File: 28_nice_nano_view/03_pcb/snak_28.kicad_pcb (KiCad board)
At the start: 2 copper layers, 114.8 x 99.6 mm, 156 parts

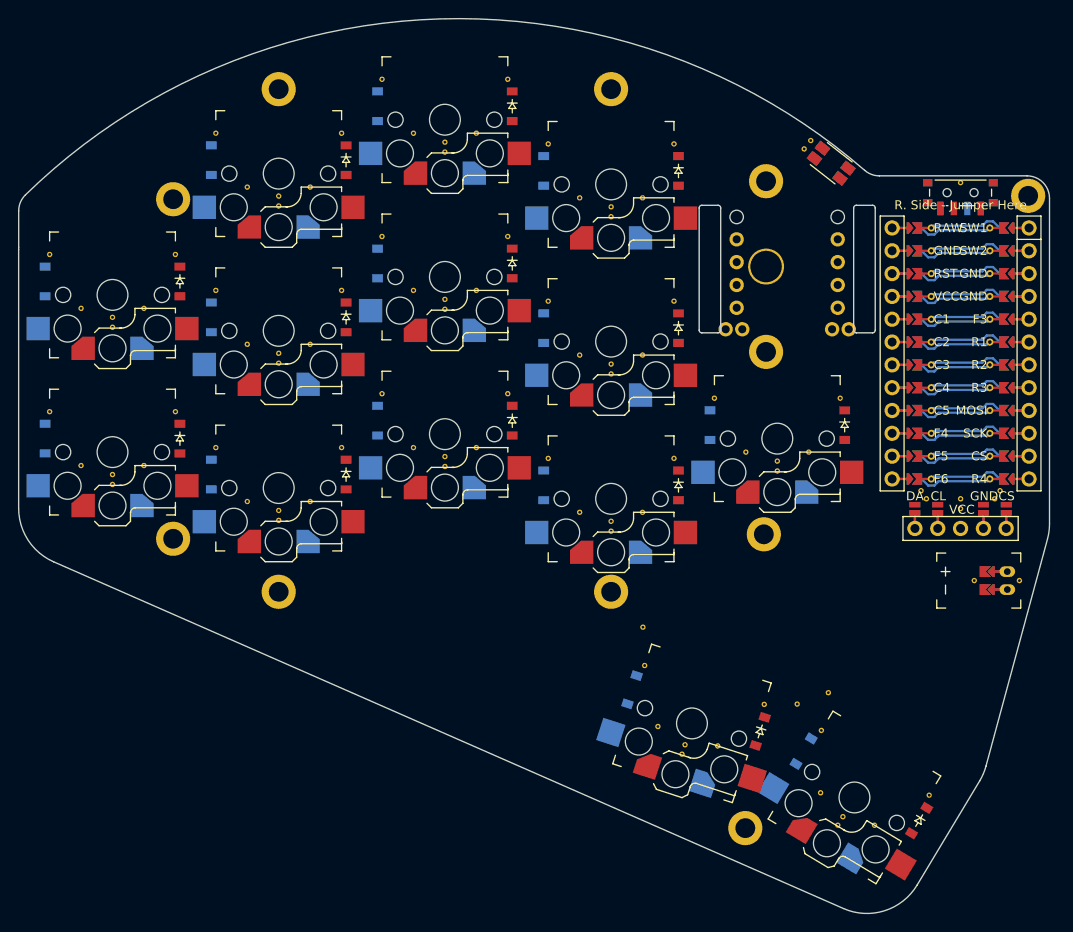
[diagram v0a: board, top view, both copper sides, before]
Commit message: add traces lib
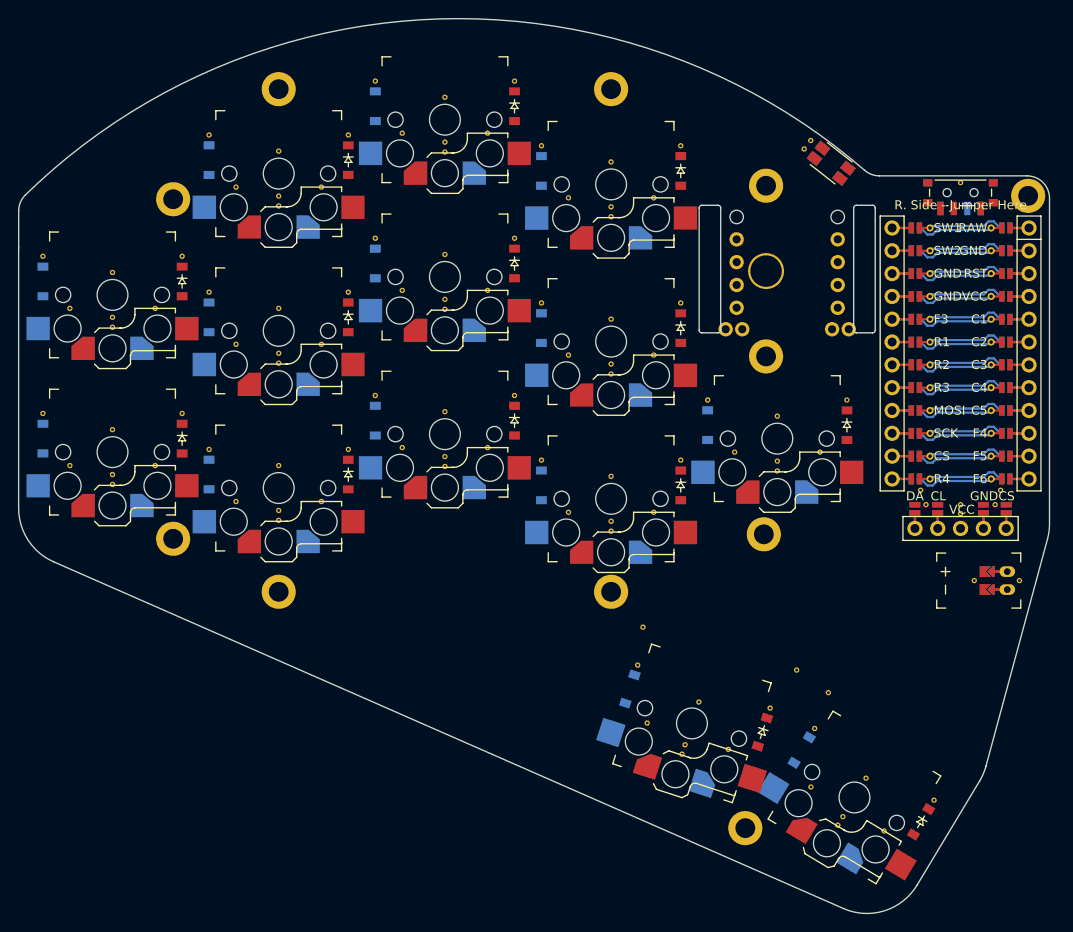
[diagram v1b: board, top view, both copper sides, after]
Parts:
- removed the REF** at (107.0, 78.0)
- removed the REF** at (162.5, 65.7)
- removed the REF** at (162.5, 48.2)
- removed the REF** at (181.0, 76.5)
- removed the REF** at (172.5, 110.6)
- removed the REF** at (190.9, 120.7)
- removed the REF** at (103.5, 84.0)
- removed the REF** at (103.5, 66.5)
- removed the REF** at (122.0, 88.0)
- removed the REF** at (122.0, 70.5)
- removed the REF** at (122.0, 53.0)
- removed the REF** at (107.0, 60.5)
- removed the REF** at (140.5, 82.0)
- removed the REF** at (140.5, 64.5)
- removed the REF** at (140.5, 47.0)
- removed the REF** at (159.0, 89.2)
- removed the REF** at (159.0, 71.7)
- removed the REF** at (159.0, 54.2)
- removed the REF** at (177.5, 82.5)
- removed the REF** at (167.4, 115.2)
- removed the REF** at (184.8, 124.0)
- removed the REF** at (93.0, 78.0)
- removed the REF** at (125.5, 82.0)
- removed the REF** at (93.0, 60.5)
- removed the REF** at (111.5, 82.0)
- removed the REF** at (111.5, 64.5)
- removed the REF** at (111.5, 47.0)
- removed the REF** at (130.0, 76.0)
- removed the REF** at (130.0, 58.5)
- removed the REF** at (130.0, 41.0)
- removed the REF** at (148.5, 83.2)
- removed the REF** at (148.5, 65.7)
- removed the REF** at (148.5, 48.2)
- removed the REF** at (125.5, 64.5)
- removed the REF** at (167.0, 76.5)
- removed the REF** at (159.2, 106.3)
- removed the REF** at (178.9, 113.5)
- removed the REF** at (96.5, 84.0)
- removed the REF** at (96.5, 66.5)
- removed the REF** at (115.0, 88.0)
- removed the REF** at (115.0, 70.5)
- removed the REF** at (115.0, 53.0)
- removed the REF** at (133.5, 82.0)
- removed the REF** at (133.5, 64.5)
- removed the REF** at (125.5, 47.0)
- removed the REF** at (133.5, 47.0)
- removed the REF** at (152.0, 89.2)
- removed the REF** at (152.0, 71.7)
- removed the REF** at (152.0, 54.2)
- removed the REF** at (170.5, 82.5)
- removed the REF** at (160.7, 113.0)
- removed the REF** at (178.8, 120.4)
- removed the REF** at (144.0, 76.0)
- removed the REF** at (144.0, 58.5)
- removed the REF** at (144.0, 41.0)
- removed the REF** at (176.2, 110.5)
- removed the REF** at (190.0, 86.8)
- removed the REF** at (198.8, 86.8)
- removed the REF** at (162.5, 83.2)
- removed the REF** at (194.4, 87.7)
- removed the REF** at (190.6, 87.7)
- removed the REF** at (198.2, 87.7)
- removed the REF** at (194.4, 88.8)
- added REF**: VIA-0.6mm, VIA-0.6mm, F.Cu at (107.8, 78.2)
- added REF**: VIA-0.6mm, VIA-0.6mm, F.Cu at (163.2, 65.9)
- added REF**: VIA-0.6mm, VIA-0.6mm, F.Cu at (190.0, 86.8)
- added REF**: VIA-0.6mm, VIA-0.6mm, F.Cu at (198.8, 86.8)
- added REF**: VIA-0.6mm, VIA-0.6mm, F.Cu at (190.6, 88.3)
- added REF**: VIA-0.6mm, VIA-0.6mm, F.Cu at (198.2, 88.3)
- added REF**: VIA-0.6mm, VIA-0.6mm, F.Cu at (194.4, 88.3)
- added REF**: VIA-0.6mm, VIA-0.6mm, F.Cu at (194.4, 89.3)
- added REF**: VIA-0.6mm, VIA-0.6mm, F.Cu at (163.2, 48.4)
- added REF**: VIA-0.6mm, VIA-0.6mm, F.Cu at (181.8, 76.7)
- added REF**: VIA-0.6mm, VIA-0.6mm, F.Cu at (173.2, 111.0)
- added REF**: VIA-0.6mm, VIA-0.6mm, F.Cu at (191.4, 121.2)
- added REF**: VIA-0.6mm, VIA-0.6mm, F.Cu at (104.8, 84.0)
- added REF**: VIA-0.6mm, VIA-0.6mm, F.Cu at (104.8, 66.5)
- added REF**: VIA-0.6mm, VIA-0.6mm, F.Cu at (123.2, 88.0)
- added REF**: VIA-0.6mm, VIA-0.6mm, F.Cu at (123.2, 70.5)
- added REF**: VIA-0.6mm, VIA-0.6mm, F.Cu at (123.2, 53.0)
- added REF**: VIA-0.6mm, VIA-0.6mm, F.Cu at (107.8, 60.7)
- added REF**: VIA-0.6mm, VIA-0.6mm, F.Cu at (141.8, 82.0)
- added REF**: VIA-0.6mm, VIA-0.6mm, F.Cu at (141.8, 64.5)
- added REF**: VIA-0.6mm, VIA-0.6mm, F.Cu at (141.8, 47.0)
- added REF**: VIA-0.6mm, VIA-0.6mm, F.Cu at (160.2, 89.2)
- added REF**: VIA-0.6mm, VIA-0.6mm, F.Cu at (160.2, 71.7)
- added REF**: VIA-0.6mm, VIA-0.6mm, F.Cu at (160.2, 54.2)
- added REF**: VIA-0.6mm, VIA-0.6mm, F.Cu at (178.8, 82.5)
- added REF**: VIA-0.6mm, VIA-0.6mm, F.Cu at (168.6, 115.6)
- added REF**: VIA-0.6mm, VIA-0.6mm, F.Cu at (185.9, 124.7)
- added REF**: VIA-0.6mm, VIA-0.6mm, F.Cu at (92.2, 78.2)
- added REF**: VIA-0.6mm, VIA-0.6mm, F.Cu at (126.2, 82.2)
- added REF**: VIA-0.6mm, VIA-0.6mm, F.Cu at (92.2, 60.7)
- added REF**: VIA-0.6mm, VIA-0.6mm, F.Cu at (110.8, 82.2)
- added REF**: VIA-0.6mm, VIA-0.6mm, F.Cu at (110.8, 64.7)
- added REF**: VIA-0.6mm, VIA-0.6mm, F.Cu at (110.8, 47.2)
- added REF**: VIA-0.6mm, VIA-0.6mm, F.Cu at (129.2, 76.2)
- added REF**: VIA-0.6mm, VIA-0.6mm, F.Cu at (129.2, 58.7)
- added REF**: VIA-0.6mm, VIA-0.6mm, F.Cu at (129.2, 41.2)
- added REF**: VIA-0.6mm, VIA-0.6mm, F.Cu at (147.8, 83.4)
- added REF**: VIA-0.6mm, VIA-0.6mm, F.Cu at (147.8, 65.9)
- added REF**: VIA-0.6mm, VIA-0.6mm, F.Cu at (147.8, 48.4)
- added REF**: VIA-0.6mm, VIA-0.6mm, F.Cu at (126.2, 64.7)
- added REF**: VIA-0.6mm, VIA-0.6mm, F.Cu at (166.2, 76.7)
- added REF**: VIA-0.6mm, VIA-0.6mm, F.Cu at (158.5, 106.2)
- added REF**: VIA-0.6mm, VIA-0.6mm, F.Cu at (178.2, 113.3)
- added REF**: VIA-0.6mm, VIA-0.6mm, F.Cu at (95.2, 84.0)
- added REF**: VIA-0.6mm, VIA-0.6mm, F.Cu at (95.2, 66.5)
- added REF**: VIA-0.6mm, VIA-0.6mm, F.Cu at (113.8, 88.0)
- added REF**: VIA-0.6mm, VIA-0.6mm, F.Cu at (113.8, 70.5)
- added REF**: VIA-0.6mm, VIA-0.6mm, F.Cu at (113.8, 53.0)
- added REF**: VIA-0.6mm, VIA-0.6mm, F.Cu at (132.2, 82.0)
- added REF**: VIA-0.6mm, VIA-0.6mm, F.Cu at (132.2, 64.5)
- added REF**: VIA-0.6mm, VIA-0.6mm, F.Cu at (126.2, 47.2)
- added REF**: VIA-0.6mm, VIA-0.6mm, F.Cu at (132.2, 47.0)
- added REF**: VIA-0.6mm, VIA-0.6mm, F.Cu at (150.8, 89.2)
- added REF**: VIA-0.6mm, VIA-0.6mm, F.Cu at (150.8, 71.7)
- added REF**: VIA-0.6mm, VIA-0.6mm, F.Cu at (150.8, 54.2)
- added REF**: VIA-0.6mm, VIA-0.6mm, F.Cu at (169.2, 82.5)
- added REF**: VIA-0.6mm, VIA-0.6mm, F.Cu at (159.5, 112.7)
- added REF**: VIA-0.6mm, VIA-0.6mm, F.Cu at (177.7, 119.8)
- added REF**: VIA-0.6mm, VIA-0.6mm, F.Cu at (144.8, 76.2)
- added REF**: VIA-0.6mm, VIA-0.6mm, F.Cu at (144.8, 58.7)
- added REF**: VIA-0.6mm, VIA-0.6mm, F.Cu at (144.8, 41.2)
- added REF**: VIA-0.6mm, VIA-0.6mm, F.Cu at (100.0, 80.0)
- added REF**: VIA-0.6mm, VIA-0.6mm, F.Cu at (100.0, 62.5)
- added REF**: VIA-0.6mm, VIA-0.6mm, F.Cu at (118.5, 84.0)
- added REF**: VIA-0.6mm, VIA-0.6mm, F.Cu at (118.5, 66.5)
- added REF**: VIA-0.6mm, VIA-0.6mm, F.Cu at (118.5, 49.0)
- added REF**: VIA-0.6mm, VIA-0.6mm, F.Cu at (163.2, 83.4)
- added REF**: VIA-0.6mm, VIA-0.6mm, F.Cu at (137.0, 78.0)
- added REF**: VIA-0.6mm, VIA-0.6mm, F.Cu at (137.0, 60.5)
- added REF**: VIA-0.6mm, VIA-0.6mm, F.Cu at (137.0, 43.0)
- added REF**: VIA-0.6mm, VIA-0.6mm, F.Cu at (155.5, 85.2)
- added REF**: VIA-0.6mm, VIA-0.6mm, F.Cu at (155.5, 67.7)
- added REF**: VIA-0.6mm, VIA-0.6mm, F.Cu at (155.5, 50.2)
- added REF**: VIA-0.6mm, VIA-0.6mm, F.Cu at (174.0, 78.5)
- added REF**: VIA-0.6mm, VIA-0.6mm, F.Cu at (165.3, 110.3)
- added REF**: VIA-0.6mm, VIA-0.6mm, F.Cu at (183.9, 118.8)
- added REF**: VIA-0.6mm, VIA-0.6mm, F.Cu at (176.2, 106.8)
- MCU1: footprint nice_nano -> ceoloide:nice_nano
- moved H5 50.3 mm to (106.8, 54.4)
- moved H6 49.1 mm to (106.8, 92.2)
- moved H3 37.0 mm to (155.5, 42.1)
- moved H4 37.0 mm to (155.5, 98.0)
- moved H1 17.0 mm to (118.5, 42.1)
- moved H2 13.1 mm to (118.5, 98.0)
- moved TP1 0.51 mm to (172.8, 62.4)
- moved D28 0.25 mm to (176.7, 115.7)
- moved D1 0.25 mm to (107.8, 81.0)
- moved D10 0.25 mm to (163.2, 68.7)
- moved D11 0.25 mm to (163.2, 51.2)
- moved D12 0.25 mm to (181.8, 79.5)
- moved D15 0.25 mm to (92.2, 81.0)
- moved D16 0.25 mm to (92.2, 63.5)
- moved D17 0.25 mm to (110.8, 85.0)
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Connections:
- MCU1 pad 1: MCU1_1 -> RAW
- MCU1 pad 10: MCU1_10 -> F4
- MCU1 pad 11: MCU1_11 -> F5
- MCU1 pad 12: MCU1_12 -> F6
- MCU1 pad 13: MCU1_13 -> MCU1_12
- MCU1 pad 14: MCU1_14 -> MCU1_11
- MCU1 pad 15: MCU1_15 -> MCU1_10
- MCU1 pad 16: MCU1_16 -> MCU1_9
- MCU1 pad 17: MCU1_17 -> MCU1_8
- MCU1 pad 18: MCU1_18 -> MCU1_7
- MCU1 pad 19: MCU1_19 -> MCU1_6
- MCU1 pad 2: MCU1_2 -> GND
- MCU1 pad 20: MCU1_20 -> MCU1_5
- MCU1 pad 21: MCU1_21 -> MCU1_4
- MCU1 pad 22: MCU1_22 -> MCU1_3
- MCU1 pad 23: MCU1_23 -> MCU1_2
- MCU1 pad 24: MCU1_24 -> MCU1_1
- MCU1 pad 3: MCU1_3 -> RST
- MCU1 pad 4: MCU1_4 -> VCC
- MCU1 pad 5: MCU1_5 -> C1
- MCU1 pad 6: MCU1_6 -> C2
- MCU1 pad 7: MCU1_7 -> C3
- MCU1 pad 8: MCU1_8 -> C4
- MCU1 pad 9: MCU1_9 -> C5
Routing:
- net C1: track 122.0 -> 14.2 mm
- net index_bot: track 121.9 -> 14.2 mm
- net R2: track 0.00 -> 101.6 mm
- net pinky_mid: track 0.00 -> 101.4 mm

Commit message: update
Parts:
- removed SW2: , sw_reset_side
- added PWR1: power_switch, ceoloide:power_switch_smd_side, F.Cu at (194.4, 53.6)
- SW1: footprint power_switch -> sw_reset_side
- moved SW1 14.8 mm to (180.0, 50.4), turned to 52 degrees
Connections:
- SW1 pad 1: (no net) -> GND
- SW1 pad 2: pos -> RST
